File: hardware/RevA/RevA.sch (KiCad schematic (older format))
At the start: 145 parts, among them J1 USB_C_Receptacle_USB2.0, J2 DNP Conn_02x02_Odd_Even, J3 DNP Conn_01x02, J4 DNP Conn_02x03_Odd_Even, J5 DNP Conn_01x02, SW1 SW_Push, SW2 SW_Push, U1 SY8120B1ABC, U10 SPI RAM LY68L6400SLIT, U2 XC6206P25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

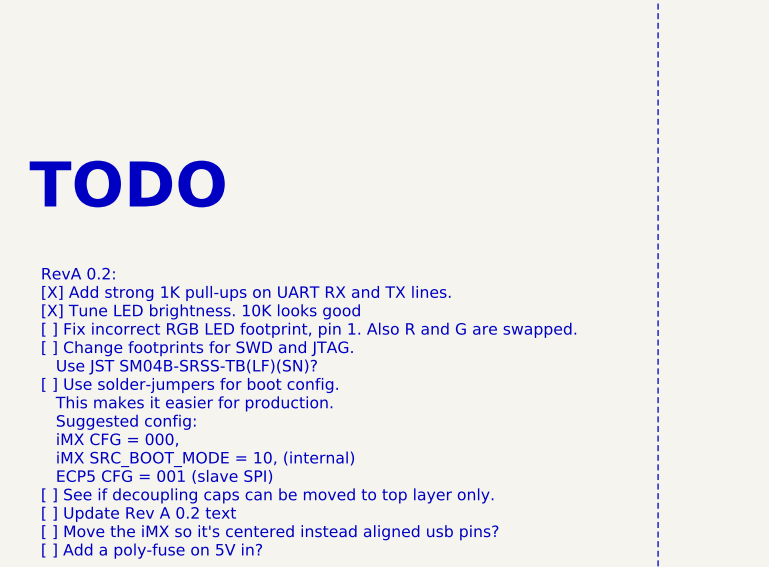
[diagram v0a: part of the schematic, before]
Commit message: hardware: Add USB TH pads solderpaste layer
This was not being done before, leading to
stencils missing the through-hole pads for
the USB connector.
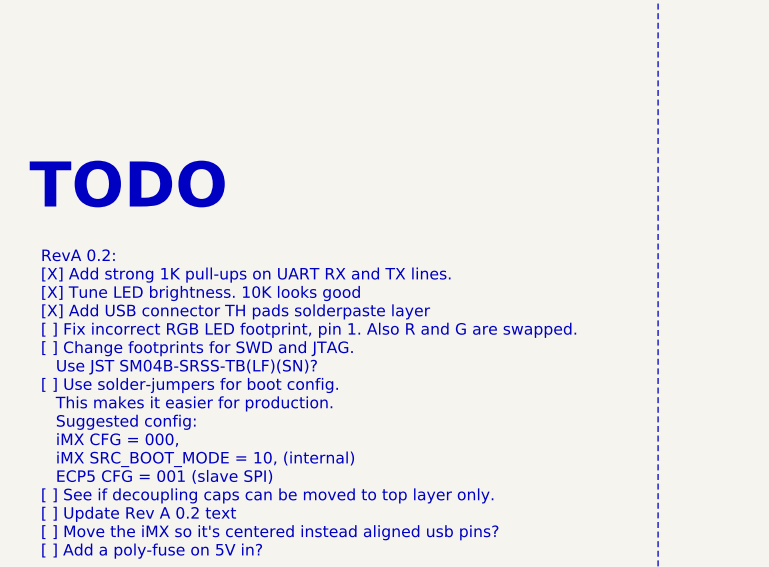
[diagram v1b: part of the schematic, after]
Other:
- note added: "RevA 0.2:\n[X] Add strong 1K pull-ups on UART RX and TX lines.\n[X] Tune LED brightness. 10K looks good\n[X] Add USB connector TH pads solderpaste layer\n[ ] Fix incorrect RGB LED footprint, pin 1. Also R and G are swapped.\n[ ] Change footprints for SWD and JTAG.\n Use JST SM04B-SRSS-TB(LF)(SN)?\n[ ] Use solder-jumpers for boot config.\n This makes it easier for production.\n Suggested config:\n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"
- note removed: "RevA 0.2:\n[X] Add strong 1K pull-ups on UART RX and TX lines.\n[X] Tune LED brightness. 10K looks good\n[ ] Fix incorrect RGB LED footprint, pin 1. Also R and G are swapped.\n[ ] Change footprints for SWD and JTAG.\n Use JST SM04B-SRSS-TB(LF)(SN)?\n[ ] Use solder-jumpers for boot config.\n This makes it easier for production.\n Suggested config:\n iMX CFG = 000,\n iMX SRC_BOOT_MODE = 10, (intern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"
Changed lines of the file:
@@
 TODO
 Text Notes 650  13950 0    50   ~ 0
-RevA 0.2:\n[X] Add strong 1K pull-ups on UART RX and TX lines.\n[X] Tune LED brightness. 10K looks good\n[ ] Fix incorrect RGB LED footprint, pin 1. Also R and G are swapped.\n[ ] Change footprints for SWD and JTAG.\n   Use JST SM04B-SRSS-TB(LF)(SN)?\n[ ] Use solder-jumpers for boot config.\n   This makes it easier for production.\n   Suggested config:\n   iMX CFG = 000,\n   iMX SRC_BOOT_MODE = 10, (internal)\n   ECP5 CFG = 001 (slave SPI)\n[ ] See if decoupling caps can be moved to top layer only.\n[ ] Update Rev A 0.2 text\n[ ] Move the iMX so it's centered instead aligned usb pins?\n[ ] Add a poly-fuse on 5V in?\n\nOptimize BOM:\n[ ] Change 220n to 100n?
+RevA 0.2:\n[X] Add strong 1K pull-ups on UART RX and TX lines.\n[X] Tune LED brightness. 10K looks good\n[X] Add USB connector TH pads solderpaste layer\n[ ] Fix incorrect RGB LED footprint, pin 1. Also R and G are swapped.\n[ ] Change footprints for SWD and JTAG.\n   Use JST SM04B-SRSS-TB(LF)(SN)?\n[ ] Use solder-jumpers for boot config.\n   This makes it easier for production.\n   Suggested config:\n   iMX CFG = 000,\n   iMX SRC_BOOT_MODE = 10, (internal)\n   ECP5 CFG = 001 (slave SPI)\n[ ] See if decoupling caps can be moved to top layer only.\n[ ] Update Rev A 0.2 text\n[ ] Move the iMX so it's centered instead aligned usb pins?\n[ ] Add a poly-fuse on 5V in?\n\nOptimize BOM:\n[ ] Change 220n to 100n?
 $Comp
 L Connector:TestPoint TP2

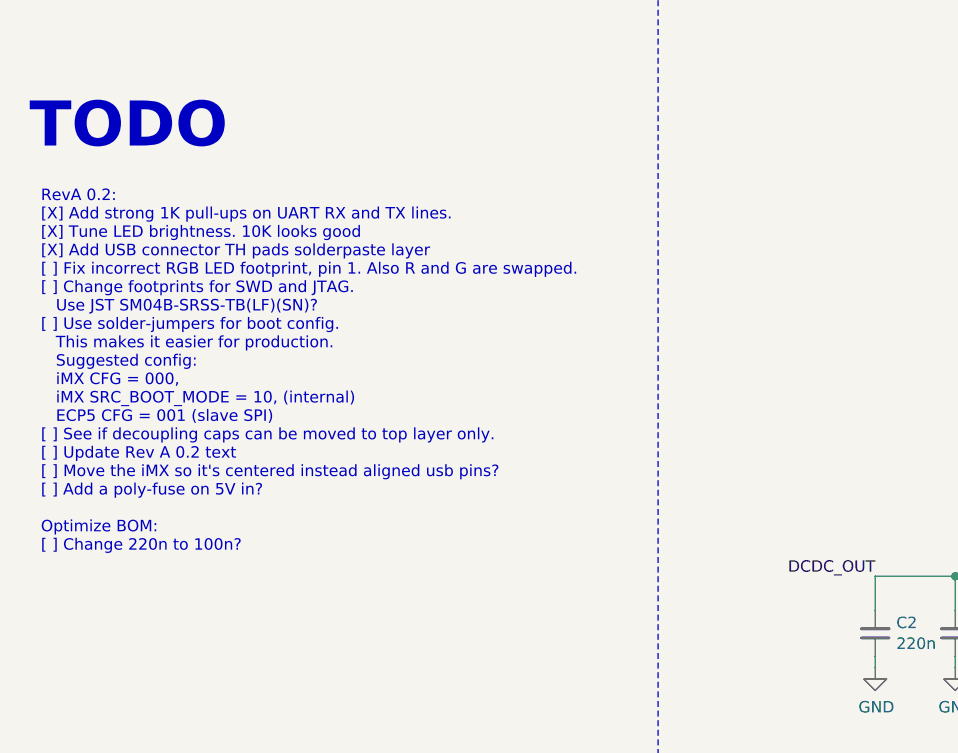
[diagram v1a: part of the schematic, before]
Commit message: hardware: Fix silkscreen for bootmode and swd
- SWD IO and CLK were swapped on the silk.
- IMX_BOOT_MODE_0 and IMX_BOOT_MODE_1 were swapped on the silk.
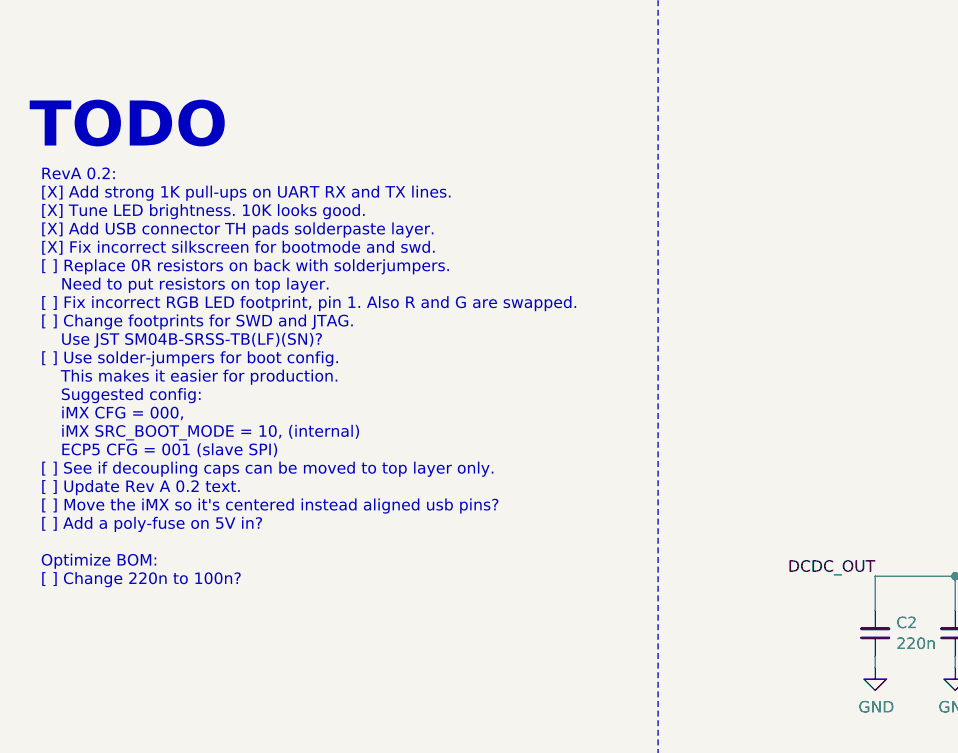
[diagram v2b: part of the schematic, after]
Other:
- note added: "RevA 0.2:\n[X] Add strong 1K pull-ups on UART RX and TX lines.\n[X] Tune LED brightness. 10K looks good.\n[X] Add USB connector TH pads solderpaste layer.\n[X] Fix incorrect silkscreen for bootmode and swd.\n[ ] Replace 0R resistors on back with solderjumpers.\n Need to put resistors on top layer.\n[ ] Fix incorrect RGB LED footprint, pin 1. Also R and G are swapped.\n[ ] Change footprints for SW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"
- note removed: "RevA 0.2:\n[X] Add strong 1K pull-ups on UART RX and TX lines.\n[X] Tune LED brightness. 10K looks good\n[X] Add USB connector TH pads solderpaste layer\n[ ] Fix incorrect RGB LED footprint, pin 1. Also R and G are swapped.\n[ ] Change footprints for SWD and JTAG.\n Use JST SM04B-SRSS-TB(LF)(SN)?\n[ ] Use solder-jumpers for boot config.\n This makes it easier for production.\n Suggested config:\n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"
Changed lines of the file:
@@
 Text Notes 600  12200 0    197  ~ 39
 TODO
-Text Notes 650  13950 0    50   ~ 0
-RevA 0.2:\n[X] Add strong 1K pull-ups on UART RX and TX lines.\n[X] Tune LED brightness. 10K looks good\n[X] Add USB connector TH pads solderpaste layer\n[ ] Fix incorrect RGB LED footprint, pin 1. Also R and G are swapped.\n[ ] Change footprints for SWD and JTAG.\n   Use JST SM04B-SRSS-TB(LF)(SN)?\n[ ] Use solder-jumpers for boot config.\n   This makes it easier for production.\n   Suggested config:\n   iMX CFG = 000,\n   iMX SRC_BOOT_MODE = 10, (internal)\n   ECP5 CFG = 001 (slave SPI)\n[ ] See if decoupling caps can be moved to top layer only.\n[ ] Update Rev A 0.2 text\n[ ] Move the iMX so it's centered instead aligned usb pins?\n[ ] Add a poly-fuse on 5V in?\n\nOptimize BOM:\n[ ] Change 220n to 100n?
+Text Notes 650  14100 0    50   ~ 0
+RevA 0.2:\n[X] Add strong 1K pull-ups on UART RX and TX lines.\n[X] Tune LED brightness. 10K looks good.\n[X] Add USB connector TH pads solderpaste layer.\n[X] Fix incorrect silkscreen for bootmode and swd.\n[ ] Replace 0R resistors on back with solderjumpers.\n    Need to put resistors on top layer.\n[ ] Fix incorrect RGB LED footprint, pin 1. Also R and G are swapped.\n[ ] Change footprints for SWD and JTAG.\n    Use JST SM04B-SRSS-TB(LF)(SN)?\n[ ] Use solder-jumpers for boot config.\n    This makes it easier for production.\n    Suggested config:\n    iMX CFG = 000,\n    iMX SRC_BOOT_MODE = 10, (internal)\n    ECP5 CFG = 001 (slave SPI)\n[ ] See if decoupling caps can be moved to top layer only.\n[ ] Update Rev A 0.2 text.\n[ ] Move the iMX so it's centered instead aligned usb pins?\n[ ] Add a poly-fuse on 5V in?\n\nOptimize BOM:\n[ ] Change 220n to 100n?
 $Comp
 L Connector:TestPoint TP2
